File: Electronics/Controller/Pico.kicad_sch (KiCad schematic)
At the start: 27 parts, among them J201 SWD, J202 Expansion, J203 USB_B_Micro, SW201 BOOT, SW202 RESET, U201 RP2040, U202 W25Q32JVSS, U203 ASDMB-12.000MHZ-LC-T

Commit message: PDF Update
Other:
- company: (none) -> findersee.fi
- title: (none) -> MQTT Output Controller
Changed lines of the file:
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@@
 (kicad_sch (version 20230121) (generator eeschema)
   (paper "A3")
+  (title_block
+    (title "MQTT Output Controller")
+    (date "2023-09-16")
+    (rev "1.0")
+    (company "findersee.fi")
+  )
   (junction (at 115.57 66.04) (diameter 0) (color 0 0 0 0)
   )

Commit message: Manufacturing Commit
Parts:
- J201: footprint Connector_PinHeader_2.54mm:PinHeader_2x02_P2.54mm_Vertical -> Connector_PinHeader_2.54mm:PinHeader_1x03_P2.54mm_Vertical
- U203: value ASDMB-12.000MHZ-LC-T -> 12MHz; footprint Oscillator:Oscillator_SMD_Abracon_ASDMB-4Pin_2.5x2.0mm -> Oscillator:Oscillator_SMD_SeikoEpson_SG8002CE-4Pin_3.2x2.5mm; Manufacturer Abracon -> (none)
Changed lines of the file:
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@@
   )
   (symbol (lib_id "Connector_Generic:Conn_01x03") (at 83.82 138.43 180) (unit 1)
-    (in_bom yes) (on_board yes) (dnp no) (fields_autoplaced)
+    (in_bom yes) (on_board yes) (dnp no)
     (property "Reference" "J201" (at 83.82 131.6101 0)
       (effects (font (size 1.27 1.27)))
@@
       (effects (font (size 1.27 1.27)))
     )
-    (property "Footprint" "Connector_PinHeader_2.54mm:PinHeader_2x02_P2.54mm_Vertical" (at 83.82 138.43 0)
+    (property "Footprint" "Connector_PinHeader_2.54mm:PinHeader_1x03_P2.54mm_Vertical" (at 83.82 138.43 0)
       (effects (font (size 1.27 1.27)) hide)
     )
@@
       (effects (font (size 1.27 1.27)))
     )
-    (property "Value" "ASDMB-12.000MHZ-LC-T" (at 55.88 92.71 0)
-      (effects (font (size 1.27 1.27)))
-    )
-    (property "Footprint" "Oscillator:Oscillator_SMD_Abracon_ASDMB-4Pin_2.5x2.0mm" (at 39.37 86.36 0)
-      (effects (font (size 1.27 1.27)) hide)
-    )
-    (property "Datasheet" "https://abracon.com/Oscillators/ASDMB.pdf" (at 46.99 74.93 0)
-      (effects (font (size 1.27 1.27)) hide)
-    )
-    (property "Manufacturer" "Abracon" (at 39.37 86.36 0)
-      (effects (font (size 1.27 1.27)) hide)
-    )
+    (property "Value" "12MHz" (at 50.8 88.9 0)
+      (effects (font (size 1.27 1.27)))
+    )
+    (property "Footprint" "Oscillator:Oscillator_SMD_SeikoEpson_SG8002CE-4Pin_3.2x2.5mm" (at 39.37 86.36 0)
+      (effects (font (size 1.27 1.27)) hide)
+    )
+    (property "Datasheet" "" (at 46.99 74.93 0)
+      (effects (font (size 1.27 1.27)) hide)
+    )
+    (property "Manufacturer" "" (at 39.37 86.36 0)
+      (effects (font (size 1.27 1.27)) hide)
+    )

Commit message: Manufacturing commit 2
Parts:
- added D303: White, LED_SMD:LED_0603_1608Metric, symbol Device:LED_Small_Filled
- added R409: 180, Resistor_SMD:R_0402_1005Metric, symbol Device:R_Small
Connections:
- net +3.3V: now also R409.2
- net at U201.39 (GPIO27): now also D303.1 (K)
- new net: D303.2 (A), R409.1
- no-connect marks 13 -> 12
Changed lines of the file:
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@@
   (junction (at 101.6 44.45) (diameter 0) (color 0 0 0 0)
   )
-  (no_connect (at 184.15 118.11))
   (no_connect (at 184.15 74.93))
   (no_connect (at 120.65 90.17))
@@
     (stroke (width 0) (type default))
   )
+  (wire (pts (xy 184.15 118.11) (xy 233.68 118.11))
+    (stroke (width 0) (type default))
+  )
   (wire (pts (xy 255.27 46.99) (xy 267.97 46.99))
     (stroke (width 0) (type default))
@@
     (stroke (width 0) (type default))
   )
+  (wire (pts (xy 233.68 106.68) (xy 233.68 107.95))
+    (stroke (width 0) (type default))
+  )
   (wire (pts (xy 115.57 68.58) (xy 120.65 68.58))
     (stroke (width 0) (type default))
@@
     (stroke (width 0) (type default))
   )
+  (wire (pts (xy 233.68 97.79) (xy 233.68 101.6))
+    (stroke (width 0) (type default))
+  )
   (wire (pts (xy 45.72 71.12) (xy 45.72 74.93))
     (stroke (width 0) (type default))
@@
   )
   (wire (pts (xy 262.89 142.24) (xy 266.7 142.24))
+    (stroke (width 0) (type default))
+  )
+  (wire (pts (xy 233.68 113.03) (xy 233.68 118.11))
     (stroke (width 0) (type default))
   )
@@
         (path "/fb53a772-8e58-43c8-9fb2-f8e622265cbb"
           (reference "C401") (unit 1)
+        )
+      )
+    )
+  )
+  (symbol (lib_id "Device:LED_Small_Filled") (at 233.68 110.49 270) (mirror x) (unit 1)
+    (in_bom yes) (on_board yes) (dnp no)
+    (property "Reference" "D303" (at 236.22 107.95 90)
+      (effects (font (size 1.27 1.27)))
+    )
+    (property "Value" "White" (at 237.49 113.03 90)
+      (effects (font (size 1.27 1.27)))
+    )
+    (property "Footprint" "LED_SMD:LED_0603_1608Metric" (at 233.68 110.49 90)
+      (effects (font (size 1.27 1.27)) hide)
+    )
+    (property "Datasheet" "~" (at 233.68 110.49 90)
+      (effects (font (size 1.27 1.27)) hide)
+    )
+    (pin "1")
+    (pin "2")
+    (instances
+      (project "Controller"
+        (path "/a2ea94cb-4178-4727-9ac9-0e597b4a505d/5e10769e-2c76-442d-969e-a77f15adcbc3"
+          (reference "D303") (unit 1)
+        )
+        (path "/a2ea94cb-4178-4727-9ac9-0e597b4a505d/7516d84f-d298-4f48-8b5d-a736b2d19d1b"
+          (reference "D403") (unit 1)
+        )
+        (path "/a2ea94cb-4178-4727-9ac9-0e597b4a505d/b4def931-2d28-466e-81ae-3813755f1fa9"
+          (reference "D201") (unit 1)
         )
       )
@@
         (path "/fb53a772-8e58-43c8-9fb2-f8e622265cbb"
           (reference "#PWR0210") (unit 1)
+        )
+      )
+    )
+  )
+  (symbol (lib_id "power:+3.3V") (at 233.68 97.79 0) (unit 1)
+    (in_bom yes) (on_board yes) (dnp no) (fields_autoplaced)
+    (property "Reference" "#PWR0218" (at 233.68 101.6 0)
+      (effects (font (size 1.27 1.27)) hide)
+    )
+    (property "Value" "+3.3V" (at 233.68 94.2881 0)
+      (effects (font (size 1.27 1.27)))
+    )
+    (property "Footprint" "" (at 233.68 97.79 0)
+      (effects (font (size 1.27 1.27)) hide)
+    )
+    (property "Datasheet" "" (at 233.68 97.79 0)
+      (effects (font (size 1.27 1.27)) hide)
+    )
+    (pin "1")
+    (instances
+      (project "Controller"
+        (path "/a2ea94cb-4178-4727-9ac9-0e597b4a505d/b4def931-2d28-466e-81ae-3813755f1fa9"
+          (reference "#PWR0218") (unit 1)
+        )
+      )
+      (project "Pico"
+        (path "/fb53a772-8e58-43c8-9fb2-f8e622265cbb"
+          (reference "#PWR0233") (unit 1)
         )
       )
@@
         )
       )
+    )
+  )
+  (symbol (lib_id "Device:R_Small") (at 233.68 104.14 180) (unit 1)
+    (in_bom yes) (on_board yes) (dnp no) (fields_autoplaced)
+    (property "Reference" "R409" (at 235.1786 103.4963 0)
+      (effects (font (size 1.27 1.27)) (justify right))
+    )
+    (property "Value" "180" (at 235.1786 105.4173 0)
+      (effects (font (size 1.27 1.27)) (justify right))
+    )
+    (property "Footprint" "Resistor_SMD:R_0402_1005Metric" (at 233.68 104.14 0)
+      (effects (font (size 1.27 1.27)) hide)
+    )
+    (property "Datasheet" "~" (at 233.68 104.14 0)
+      (effects (font (size 1.27 1.27)) hide)
+    )
+    (pin "1")
+    (pin "2")
+    (instances
+      (project "Controller"
+        (path "/a2ea94cb-4178-4727-9ac9-0e597b4a505d/7516d84f-d298-4f48-8b5d-a736b2d19d1b"
+          (reference "R409") (unit 1)
+        )
+        (path "/a2ea94cb-4178-4727-9ac9-0e597b4a505d/b4def931-2d28-466e-81ae-3813755f1fa9"
+          (reference "R203") (unit 1)
+        )
+      )

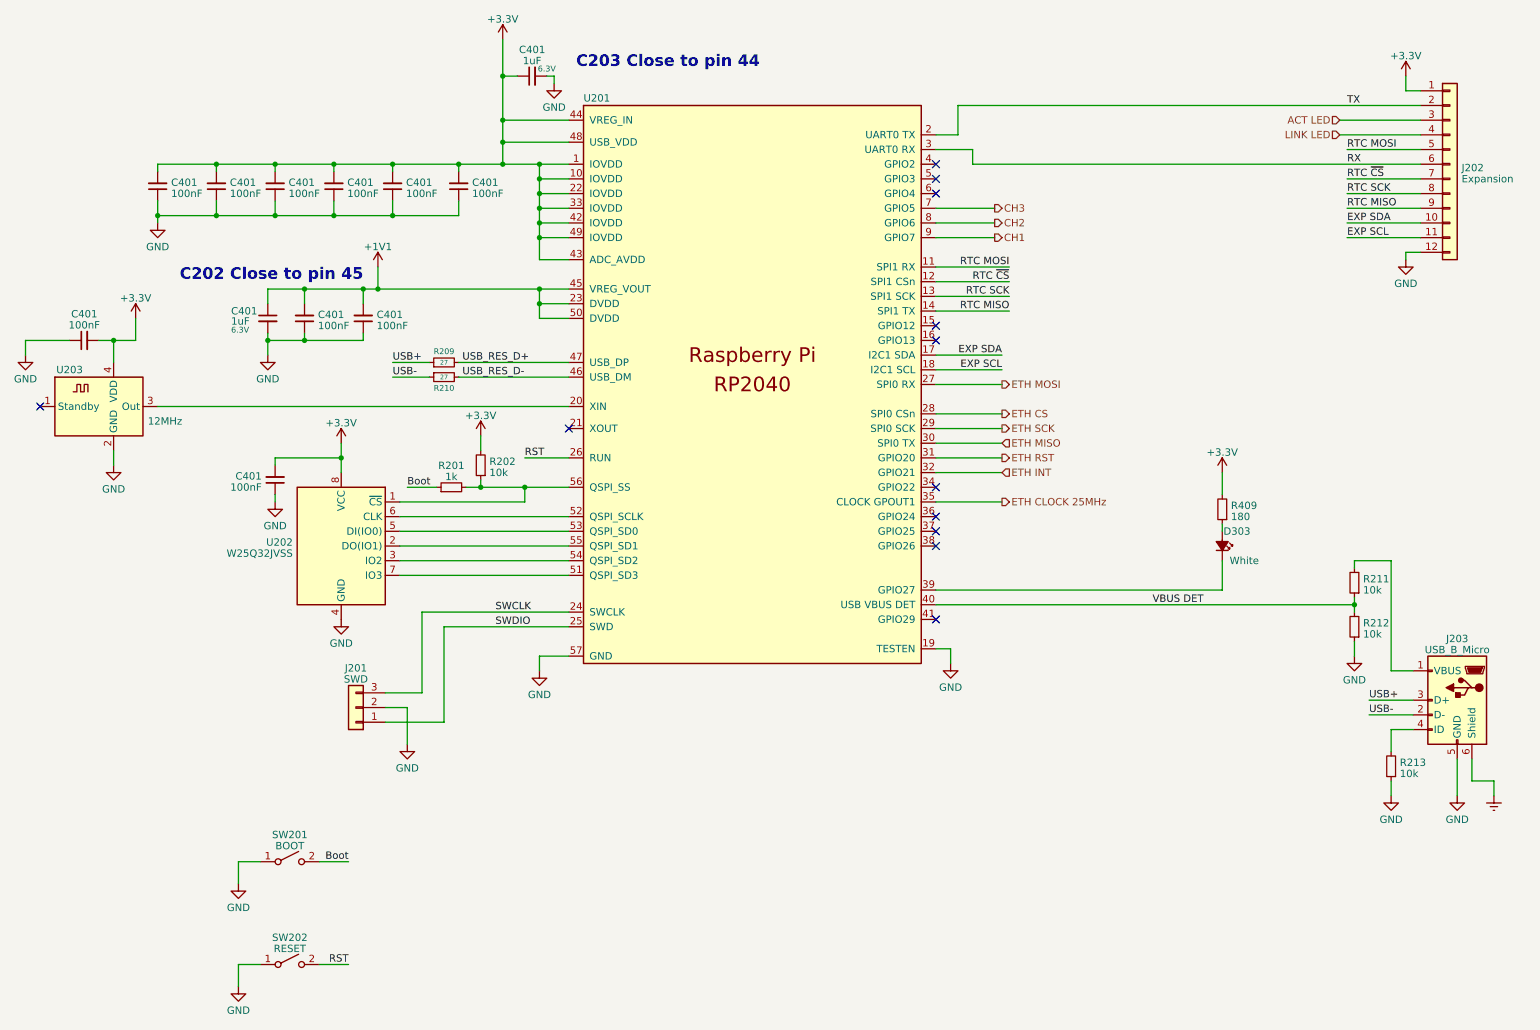
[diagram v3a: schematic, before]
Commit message: Pin goof fix
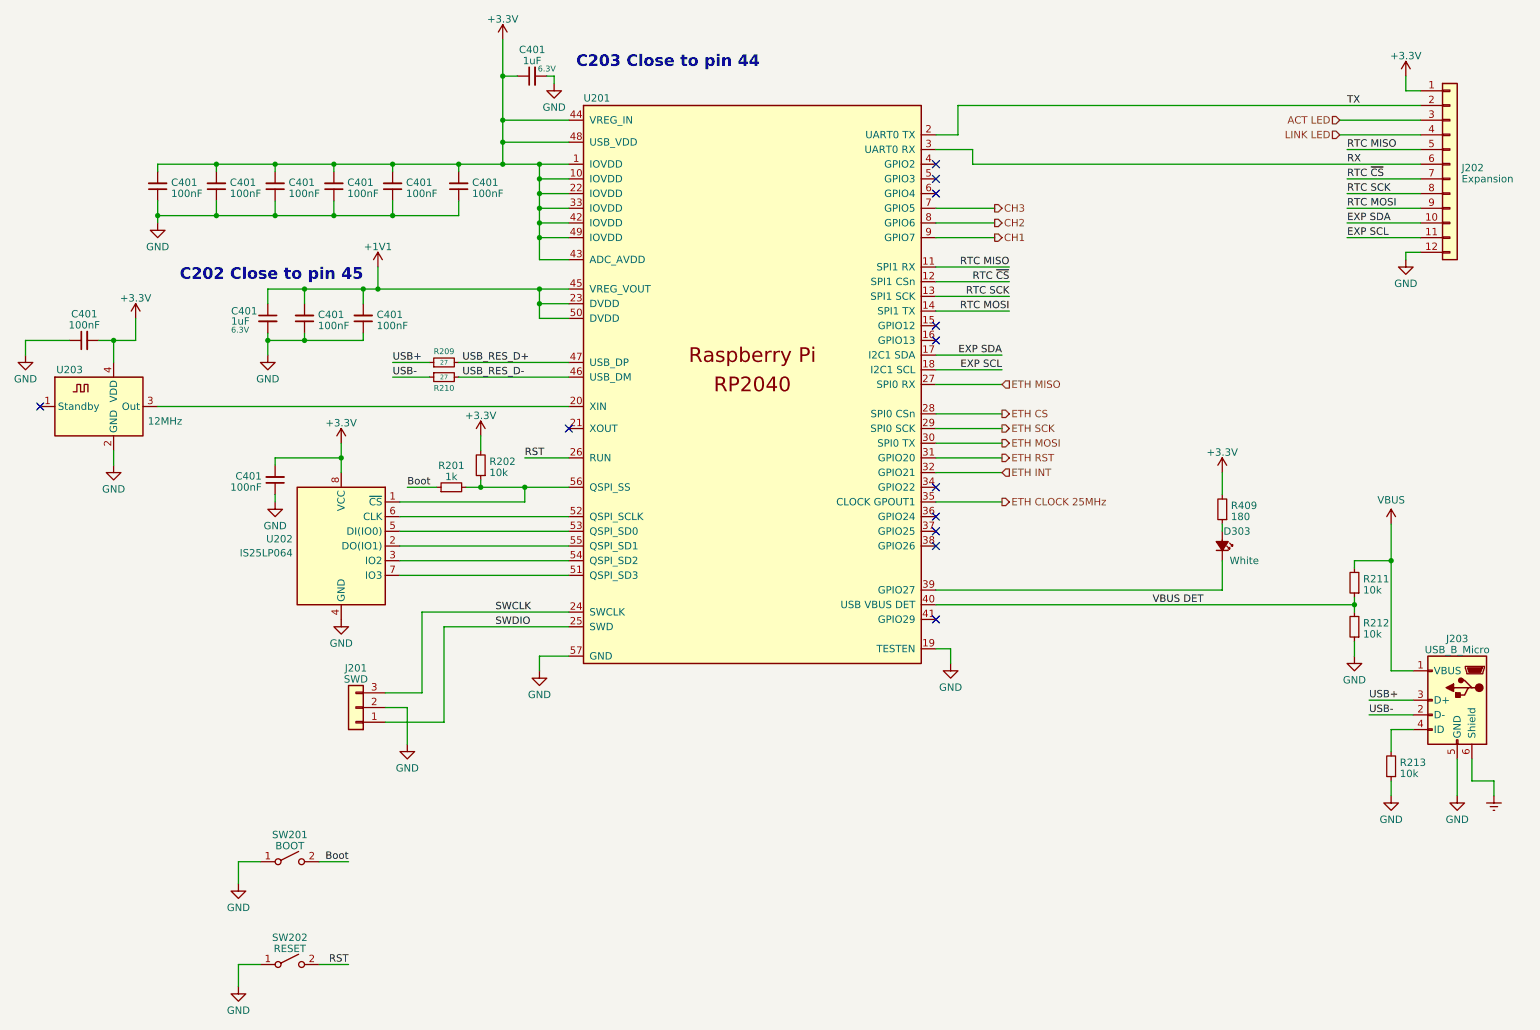
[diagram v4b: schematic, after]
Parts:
- R209, R210: now in the parts list
- U202: value W25Q32JVSS -> IS25LP064
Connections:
- net ETH MISO: now also U201.27 (GPIO16); no longer U201.30 (GPIO19)
- net ETH MOSI: now also U201.30 (GPIO19); no longer U201.27 (GPIO16)
- net RTC MISO: now also J202.5 (Pin_5), U201.11 (GPIO8); no longer J202.9 (Pin_9), U201.14 (GPIO11)
- net RTC MOSI: now also J202.9 (Pin_9), U201.14 (GPIO11); no longer J202.5 (Pin_5), U201.11 (GPIO8)
- net VBUS: now reaches J203.1 (VBUS), R211.2
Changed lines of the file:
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@@
   (junction (at 59.69 53.34) (diameter 0) (color 0 0 0 0)
+  )
+  (junction (at 262.89 113.03) (diameter 0) (color 0 0 0 0)
   )
   (junction (at 115.57 57.15) (diameter 0) (color 0 0 0 0)
@@
     (stroke (width 0) (type default))
   )
+  (wire (pts (xy 262.89 106.68) (xy 262.89 113.03))
+    (stroke (width 0) (type default))
+  )
   (wire (pts (xy 120.65 57.15) (xy 115.57 57.15))
     (stroke (width 0) (type default))
@@
     (effects (font (size 1.27 1.27)) (justify left bottom))
   )
-  (label "RTC MOSI" (at 255.27 41.91 0) (fields_autoplaced)
+  (label "RTC MOSI" (at 255.27 52.07 0) (fields_autoplaced)
     (effects (font (size 1.27 1.27)) (justify left bottom))
   )
@@
     (effects (font (size 1.27 1.27)) (justify right bottom))
   )
-  (label "RTC MOSI" (at 196.85 62.23 180) (fields_autoplaced)
+  (label "RTC MOSI" (at 196.85 69.85 180) (fields_autoplaced)
     (effects (font (size 1.27 1.27)) (justify right bottom))
   )
@@
     (effects (font (size 1.27 1.27)) (justify right bottom))
   )
-  (label "RTC MISO" (at 196.85 69.85 180) (fields_autoplaced)
+  (label "RTC MISO" (at 196.85 62.23 180) (fields_autoplaced)
     (effects (font (size 1.27 1.27)) (justify right bottom))
   )
@@
     (effects (font (size 1.27 1.27)) (justify left bottom))
   )
-  (label "RTC MISO" (at 255.27 52.07 0) (fields_autoplaced)
+  (label "RTC MISO" (at 255.27 41.91 0) (fields_autoplaced)
     (effects (font (size 1.27 1.27)) (justify left bottom))
   )
@@
     (effects (font (size 1.27 1.27)) (justify left))
   )
-  (hierarchical_label "ETH MISO" (shape input) (at 195.58 92.71 0) (fields_autoplaced)
+  (hierarchical_label "ETH MISO" (shape input) (at 195.58 82.55 0) (fields_autoplaced)
     (effects (font (size 1.27 1.27)) (justify left))
   )
-  (hierarchical_label "ETH MOSI" (shape output) (at 195.58 82.55 0) (fields_autoplaced)
+  (hierarchical_label "ETH MOSI" (shape output) (at 195.58 92.71 0) (fields_autoplaced)
     (effects (font (size 1.27 1.27)) (justify left))
   )
@@
     )
   )
+  (symbol (lib_id "power:VBUS") (at 262.89 106.68 0) (unit 1)
+    (in_bom yes) (on_board yes) (dnp no) (fields_autoplaced)
+    (property "Reference" "#PWR0404" (at 262.89 110.49 0)
+      (effects (font (size 1.27 1.27)) hide)
+    )
+    (property "Value" "VBUS" (at 262.89 102.5469 0)
+      (effects (font (size 1.27 1.27)))
+    )
+    (property "Footprint" "" (at 262.89 106.68 0)
+      (effects (font (size 1.27 1.27)) hide)
+    )
+    (property "Datasheet" "" (at 262.89 106.68 0)
+      (effects (font (size 1.27 1.27)) hide)
+    )
+    (pin "1")
+    (instances
+      (project "Controller"
+        (path "/a2ea94cb-4178-4727-9ac9-0e597b4a505d/7516d84f-d298-4f48-8b5d-a736b2d19d1b"
+          (reference "#PWR0404") (unit 1)
+        )
+        (path "/a2ea94cb-4178-4727-9ac9-0e597b4a505d/b4def931-2d28-466e-81ae-3813755f1fa9"
+          (reference "#PWR0219") (unit 1)
+        )
+      )
+    )
+  )
   (symbol (lib_id "power:GND") (at 26.67 77.47 0) (unit 1)
     (in_bom yes) (on_board yes) (dnp no) (fields_autoplaced)
@@
   )
   (symbol (lib_id "Device:R_Small") (at 99.06 81.28 90) (mirror x) (unit 1)
-    (in_bom no) (on_board yes) (dnp no)
+    (in_bom yes) (on_board yes) (dnp no)
     (property "Reference" "R210" (at 99.06 83.185 90)
       (effects (font (size 1 1)))
@@
   )
   (symbol (lib_id "Device:R_Small") (at 99.06 78.74 90) (unit 1)
-    (in_bom no) (on_board yes) (dnp no)
+    (in_bom yes) (on_board yes) (dnp no)
     (property "Reference" "R209" (at 99.06 76.835 90)
       (effects (font (size 1 1)))
@@
   (symbol (lib_id "Memory_Flash:W25Q32JVSS") (at 81.28 110.49 0) (mirror y) (unit 1)
     (in_bom yes) (on_board yes) (dnp no) (fields_autoplaced)
-    (property "Reference" "U202" (at 72.8981 109.8463 0)
+    (property "Reference" "U202" (at 72.8981 109.2779 0)
       (effects (font (size 1.27 1.27)) (justify left))
     )
-    (property "Value" "W25Q32JVSS" (at 72.8981 111.7673 0)
+    (property "Value" "IS25LP064" (at 72.8981 111.7021 0)
       (effects (font (size 1.27 1.27)) (justify left))
     )

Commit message: Added library Fixed layout bugs Software improvements
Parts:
- C401: symbol Device:C_Small -> Capacitors_0402:CAPC_100nF_X5R_16V_0402; Material (none) -> X5R; Voltage (none) -> 16V
- C401: symbol Device:C_Small -> Capacitors_0402:CAPC_1uF_X5R_10V_0402; Material (none) -> X5R; Voltage 6.3V -> 10V
- R201: symbol Device:R_Small -> Resistors_0402:RESC_0402_1k; Package (none) -> 0402
- R202, R211, R212: symbol Device:R_Small -> Resistors_0402:RESC_0402_10k; Package (none) -> 0402; now in the parts list
- R209, R210: symbol Device:R_Small -> Resistors_0402:RESC_0402_27R4; Package (none) -> 0402
- R409: value 180 -> 187R; symbol Device:R_Small -> Resistors_0402:RESC_0402_187R; Package (none) -> 0402
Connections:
- net EXP SCL renamed EXP IO1
- net EXP SDA renamed EXP IO0

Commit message: Improvements
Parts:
- renumbered C401 to C201, C401 to C202, C401 to C203, C401 to C204, C401 to C205, C401 to C206, C401 to C207, C401 to C208, C401 to C209, C401 to C210, C401 to C211, C401 to C215, D303 to D201, R409 to R203
